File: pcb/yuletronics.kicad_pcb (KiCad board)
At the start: 2 copper layers, 45 x 50 mm, 35 parts, among them IC1 STM32F042F6P6, IC2 MCP1700, IC3 TLV61225, J1 BATT, J2 MICROUSB, P1 SWD_TC, SW1 BOOTLOAD, SW2 PWR_SWITCH

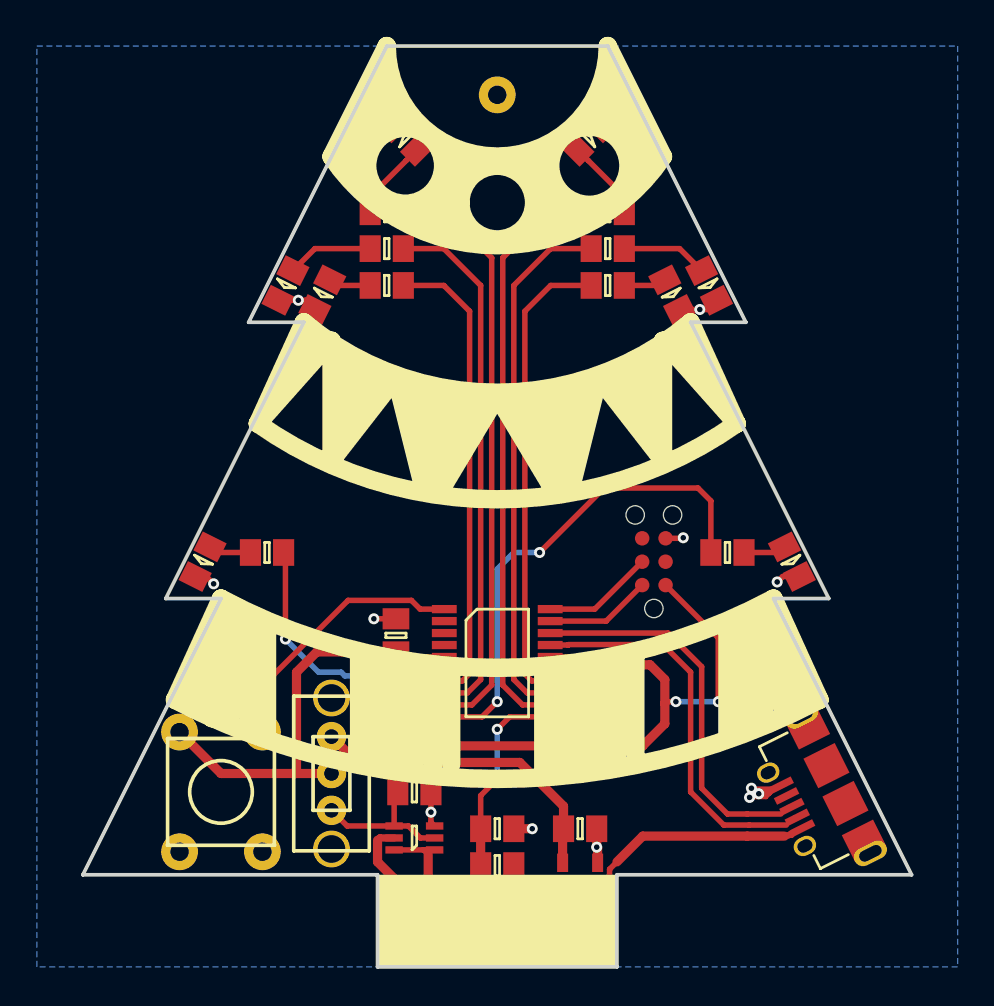
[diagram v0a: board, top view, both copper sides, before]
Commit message: Add LED array
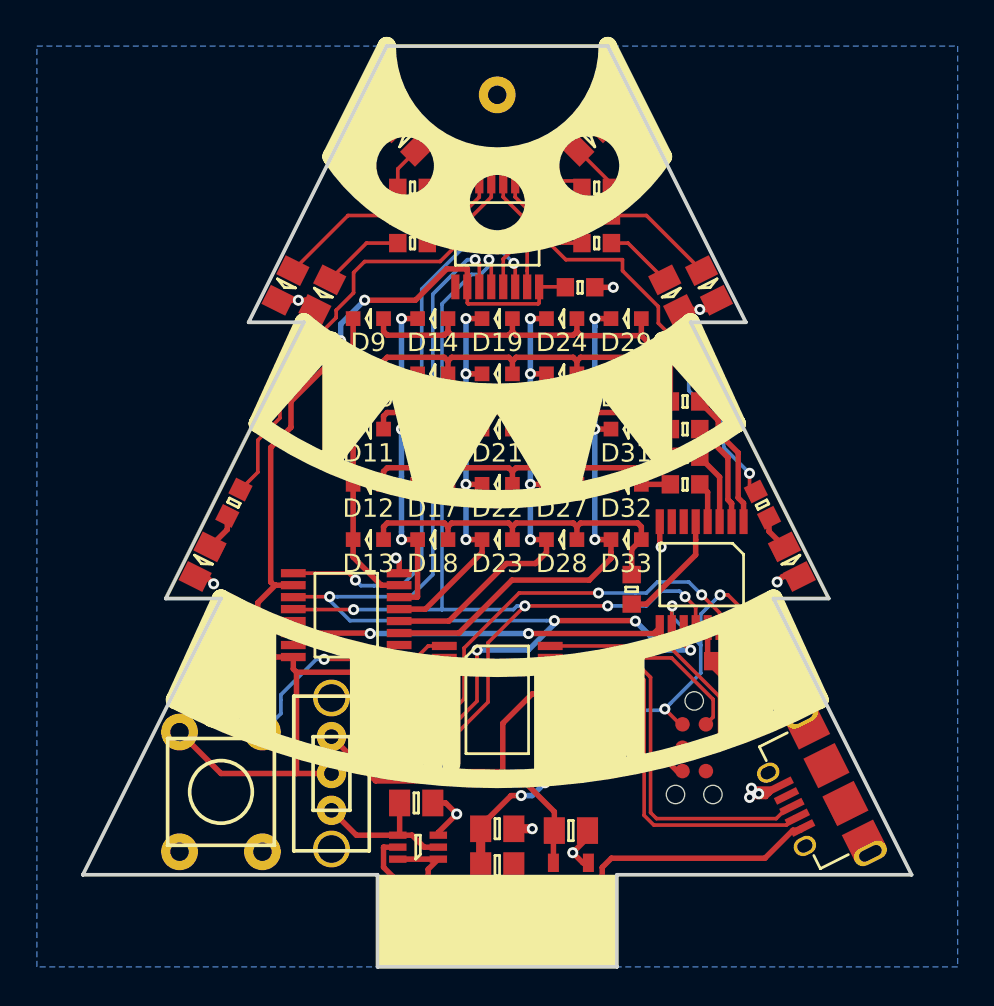
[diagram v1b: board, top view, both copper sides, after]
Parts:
- added C10: 100n, agg:0603, F.Cu at (142.5, 118.4)
- added C8: 100n, agg:0603, F.Cu at (134.5, 98.1)
- added C9: 100n, agg:0603, F.Cu at (116.3, 117.7)
- added D10: LED, kpt-1608:KPT-1608, F.Cu at (123.0, 102.8)
- added D11: LED, kpt-1608:KPT-1608, F.Cu at (123.0, 105.8)
- added D12: LED, kpt-1608:KPT-1608, F.Cu at (123.0, 108.8)
- added D13: LED, kpt-1608:KPT-1608, F.Cu at (123.0, 111.8)
- added D14: LED, kpt-1608:KPT-1608, F.Cu at (126.5, 99.8)
- added D15: LED, kpt-1608:KPT-1608, F.Cu at (126.5, 102.8)
- added D16: LED, kpt-1608:KPT-1608, F.Cu at (126.5, 105.8)
- added D17: LED, kpt-1608:KPT-1608, F.Cu at (126.5, 108.8)
- added D18: LED, kpt-1608:KPT-1608, F.Cu at (126.5, 111.8)
- added D19: LED, kpt-1608:KPT-1608, F.Cu at (130.0, 99.8)
- added D20: LED, kpt-1608:KPT-1608, F.Cu at (130.0, 102.8)
- added D21: LED, kpt-1608:KPT-1608, F.Cu at (130.0, 105.8)
- added D22: LED, kpt-1608:KPT-1608, F.Cu at (130.0, 108.8)
- added D23: LED, kpt-1608:KPT-1608, F.Cu at (130.0, 111.8)
- added D24: LED, kpt-1608:KPT-1608, F.Cu at (133.5, 99.8)
- added D25: LED, kpt-1608:KPT-1608, F.Cu at (133.5, 102.8)
- added D26: LED, kpt-1608:KPT-1608, F.Cu at (133.5, 105.8)
- added D27: LED, kpt-1608:KPT-1608, F.Cu at (133.5, 108.8)
- added D28: LED, kpt-1608:KPT-1608, F.Cu at (133.5, 111.8)
- added D29: LED, kpt-1608:KPT-1608, F.Cu at (137.0, 99.8)
- added D30: LED, kpt-1608:KPT-1608, F.Cu at (137.0, 102.8)
- added D31: LED, kpt-1608:KPT-1608, F.Cu at (137.0, 105.8)
- added D32: LED, kpt-1608:KPT-1608, F.Cu at (137.0, 108.8)
- added D33: LED, kpt-1608:KPT-1608, F.Cu at (137.0, 111.8)
- added D9: LED, kpt-1608:KPT-1608, F.Cu at (123.0, 99.8)
- added IC4: 74HC595, agg:TSSOP-16, F.Cu at (130.0, 95.2)
- added IC5: 74HC595, agg:TSSOP-16, F.Cu at (141.1, 113.7)
- added IC6: 74HC595, agg:TSSOP-16, F.Cu at (121.8, 115.9)
- added R12: 330R, agg:0603, F.Cu at (140.2, 104.3)
- added R13: 330R, agg:0603, F.Cu at (140.2, 105.8)
- added R14: 330R, agg:0603, F.Cu at (140.2, 107.3)
- added R15: 330R, agg:0603, F.Cu at (140.2, 108.8)
- added R16: 330R, agg:0603, F.Cu at (137.3, 114.5)
- R10, R9: value R -> 330R; footprint agg:0805 -> agg:0603
- R11: value R -> 330; footprint agg:0805 -> agg:0603
- R4, R5, R6, R7, R8: footprint agg:0805 -> agg:0603
- moved P1 10.3 mm to (140.7, 123.1), turned to 270 degrees
- moved C3 4.03 mm to (125.0, 121.0), turned to 90 degrees
- moved R4 3.24 mm to (115.7, 109.8), turned to 243.4 degrees
- moved R8 3.22 mm to (144.4, 109.9), turned to 296.6 degrees
- moved R5 2.69 mm to (125.4, 95.7)
- moved R11 2.38 mm to (135.4, 95.7)
- moved R6 2.28 mm to (125.4, 94.2)
- moved IC1 2.00 mm to (130.0, 120.5)
- moved R7 1.91 mm to (125.4, 92.7)
- moved R10 1.90 mm to (135.4, 94.2)
- moved C1 1.60 mm to (137.0, 121.1)
- moved C2 1.60 mm to (135.0, 121.1)
- moved R9 1.43 mm to (135.4, 92.7)
- moved C7 0.61 mm to (125.6, 126.1)
- moved IC3 0.54 mm to (125.7, 128.5)
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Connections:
- IC1 pad 10: /LED5 -> Net-(IC1-Pad10)
- IC1 pad 12: /LED6 -> Net-(IC1-Pad12)
- IC1 pad 13: /LED7 -> Net-(IC1-Pad13)
- IC1 pad 14: /LED8 -> Net-(IC1-Pad14)
- IC1 pad 6: /LED1 -> /SHIFT_IN
- IC1 pad 7: /LED2 -> /SHIFT_CLK
- IC1 pad 8: /LED3 -> /SHIFT_STORE
- IC1 pad 9: /LED4 -> Net-(IC1-Pad9)
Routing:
- net /SHIFT_CLK: track 0.00 -> 60.1 mm, vias 0 -> 6
- net /SHIFT_STORE: track 0.00 -> 54.7 mm, vias 0 -> 5
- net 3v3: track 63.9 -> 105.5 mm, vias 2 -> 6
- net /COL5: track 0.00 -> 30.6 mm, vias 0 -> 5
- net Net-(IC4-Pad14): track 0.00 -> 30.2 mm, vias 0 -> 2
- net /LED6: track 32.1 -> 2.48 mm
- net /LED4: track 32.1 -> 3.31 mm
- net /COL4: track 0.00 -> 26.6 mm, vias 0 -> 5
- net /LED3: track 28.7 -> 4.11 mm
- net /LED7: track 28.7 -> 4.26 mm
- net /COL3: track 0.00 -> 22.8 mm, vias 0 -> 5
- net Net-(D14-Pad2): track 0.00 -> 22.5 mm
- net Net-(D10-Pad2): track 0.00 -> 21.9 mm
- net /SHIFT_IN: track 0.00 -> 20.8 mm, vias 0 -> 2
- net /COL2: track 0.00 -> 20.5 mm, vias 0 -> 5
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
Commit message: Add gerbers, fix DRC
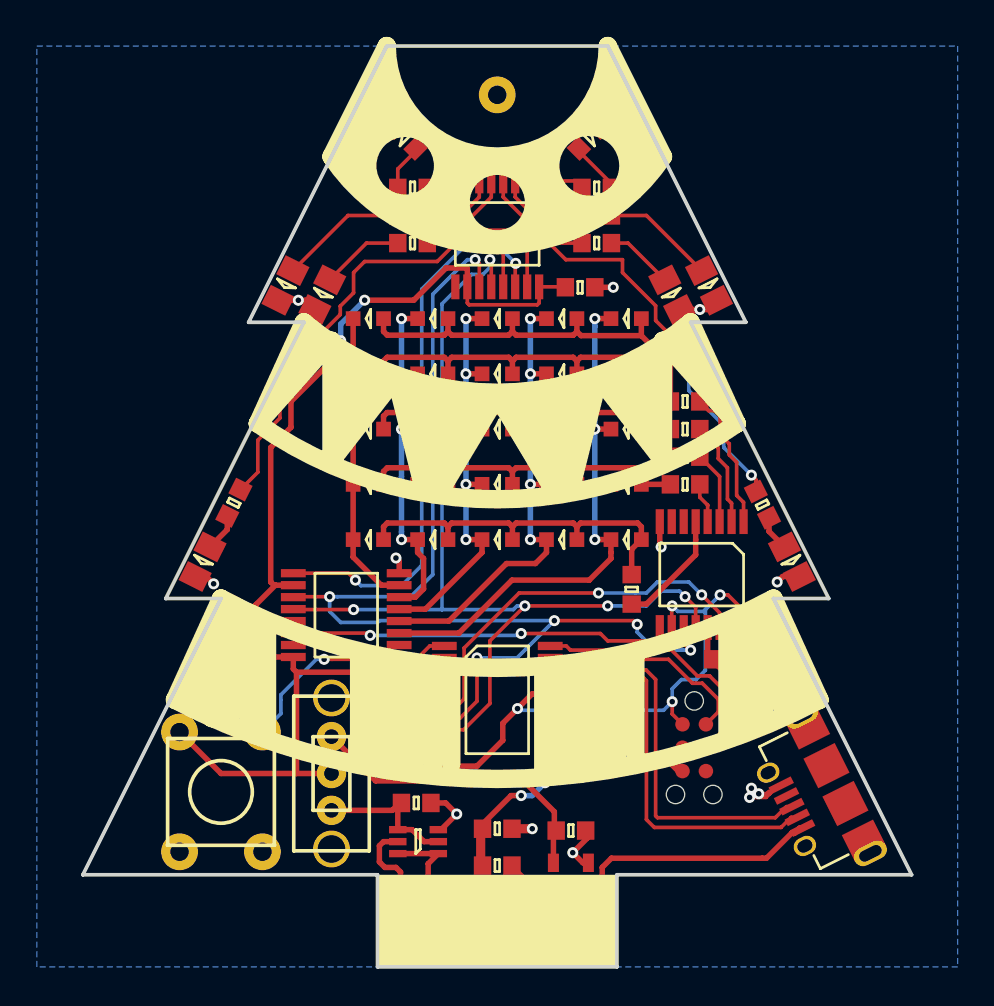
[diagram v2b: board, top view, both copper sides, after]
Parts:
- C1, C4, C7: value 10µ -> 10u; footprint agg:0805 -> agg:0603
- C2, C3, R1, R2, R3: footprint agg:0805 -> agg:0603
- C5, C6: value 1µ -> 1u; footprint agg:0805 -> agg:0603
- D4, D6: footprint agg:0805-LED -> kpa-1606:KPA-1606
- L1: value 4µ7 -> 4u7
- R11: value 330 -> 330R
- R4, R5, R6, R7, R8: value R -> 330R
- moved IC3 0.30 mm to (125.7, 128.2)
- moved C10 0.10 mm to (142.5, 118.3)
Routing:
- net 3v3: track 105.5 -> 108.2 mm
- net GND: track 47.0 -> 44.8 mm
- net Net-(IC5-Pad9): track 20.0 -> 20.8 mm
- net /SWCLK: track 13.4 -> 14.1 mm
- net /BATT_3V3: track 8.42 -> 7.83 mm
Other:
- net class Default: clearance 0.15 -> 0.2; trace_width 0.15 -> 0.2
- rule trace_clearance: 0.15 -> 0.2
- rule trace_min: 0.15 -> 0.2
- board text added: "J. Wood 2016"
